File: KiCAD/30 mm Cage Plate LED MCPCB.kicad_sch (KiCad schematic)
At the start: 14 parts, among them IC1 AL8843QSP-13, J1 Conn_01x04

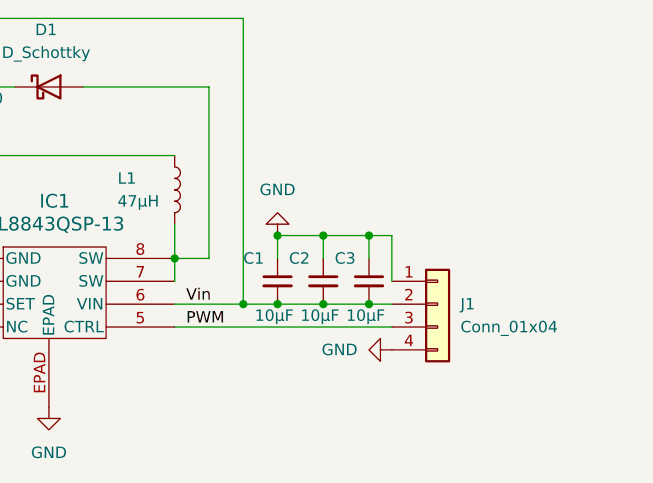
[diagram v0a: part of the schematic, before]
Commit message: Move PWM and Vin pins apart to prevent fatal shorts of Vin to Ctrl
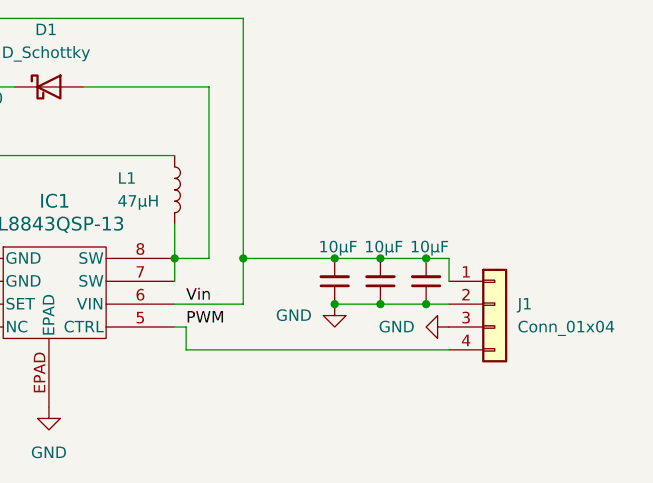
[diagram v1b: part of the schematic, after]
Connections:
- net GND: now also J1.2 (Pin_2), J1.3 (Pin_3); no longer J1.1 (Pin_1), J1.4 (Pin_4)
- net PWM: now also J1.4 (Pin_4); no longer J1.3 (Pin_3)
- net Vin: now also J1.1 (Pin_1); no longer J1.2 (Pin_2)
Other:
- moved on the sheet: J1

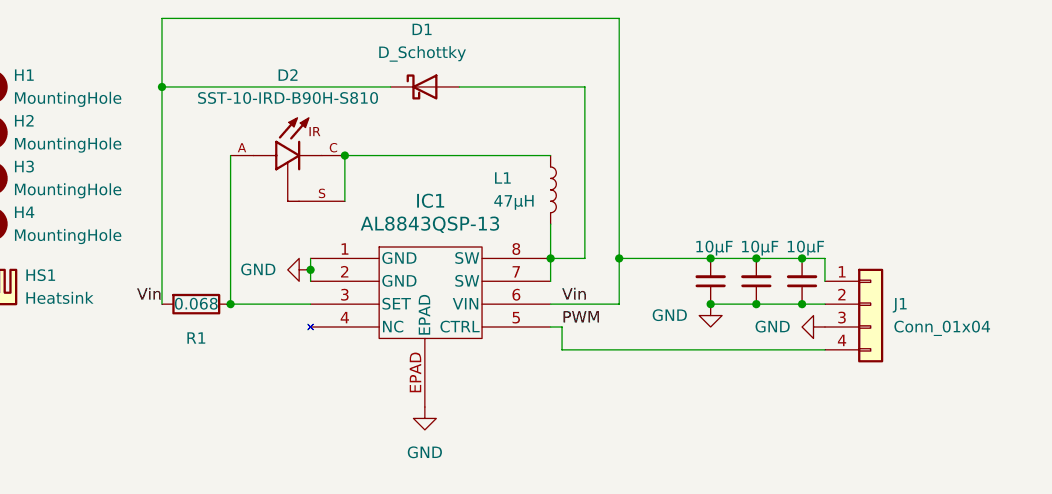
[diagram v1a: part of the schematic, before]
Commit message: Imrpoved design - more caps and therm
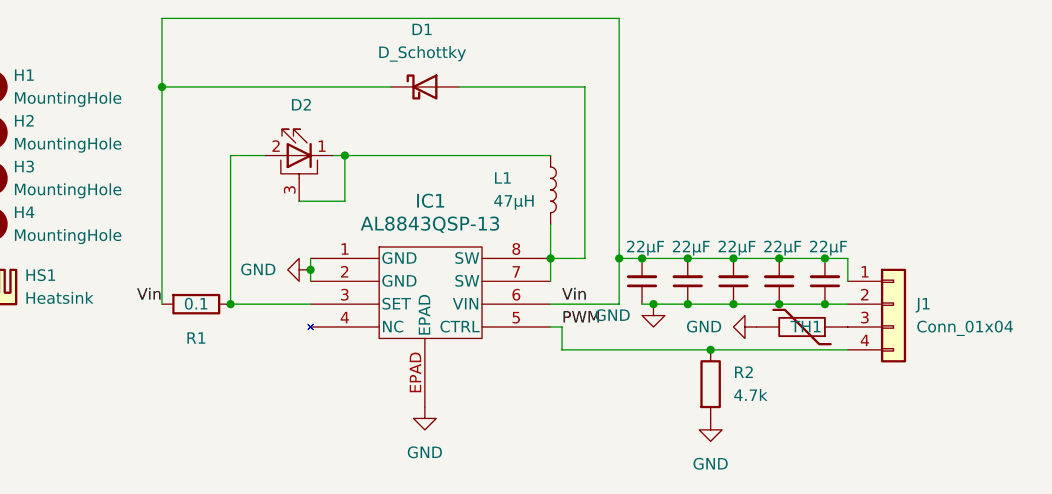
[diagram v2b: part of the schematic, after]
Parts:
- added C4, C5: 22µF, Capacitor_SMD:C_0805_2012Metric, symbol Device:C_Small
- added R2: 4.7k, Capacitor_SMD:C_0603_1608Metric, symbol Device:R
- added TH1: Thermistor, Resistor_SMD:R_0603_1608Metric, symbol Device:Thermistor
- C1, C2, C3: value 10μF -> 22µF; footprint Capacitor_SMD:C_0603_1608Metric -> Capacitor_SMD:C_0805_2012Metric; Manufacturer Murata Electronics -> Samsung Electro-Mechanics; Part GRM188R6YA106MA73D -> CL21A226MAYNNNE
- D2: footprint Custom:LED_SST-10-IRD-B90H-S810 -> Custom:CSSRML_C69062_AOS; symbol Custom:SST-10-IRD-B90H-S810 -> Device:LED_Pad; Manufacturer Luminus Devices Inc. -> ams-OSRAM USA INC.; Part SST-10-IRD-B90H-S810 -> GF CSSRML.24-TNUL-1-1-350-R33
- R1: value 0.068 -> 0.1; Manufacturer Ohmite -> Thin Film Technology Corp.; Part KDV12FR068ET -> D1WRL1206L4R100D-T5
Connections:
- net GND: now also C4.1, C5.1, R2.2, TH1.2; no longer J1.3 (Pin_3)
- net PWM: now also R2.1
- net Vin: now also C4.2, C5.2
- net at IC1.3 (SET), R1.1: now also D2.2 (A); no longer D2.A
- new net: J1.3 (Pin_3), TH1.1
- new net: D2.1 (K), D2.3 (PAD), L1.1
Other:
- moved on the sheet: J1

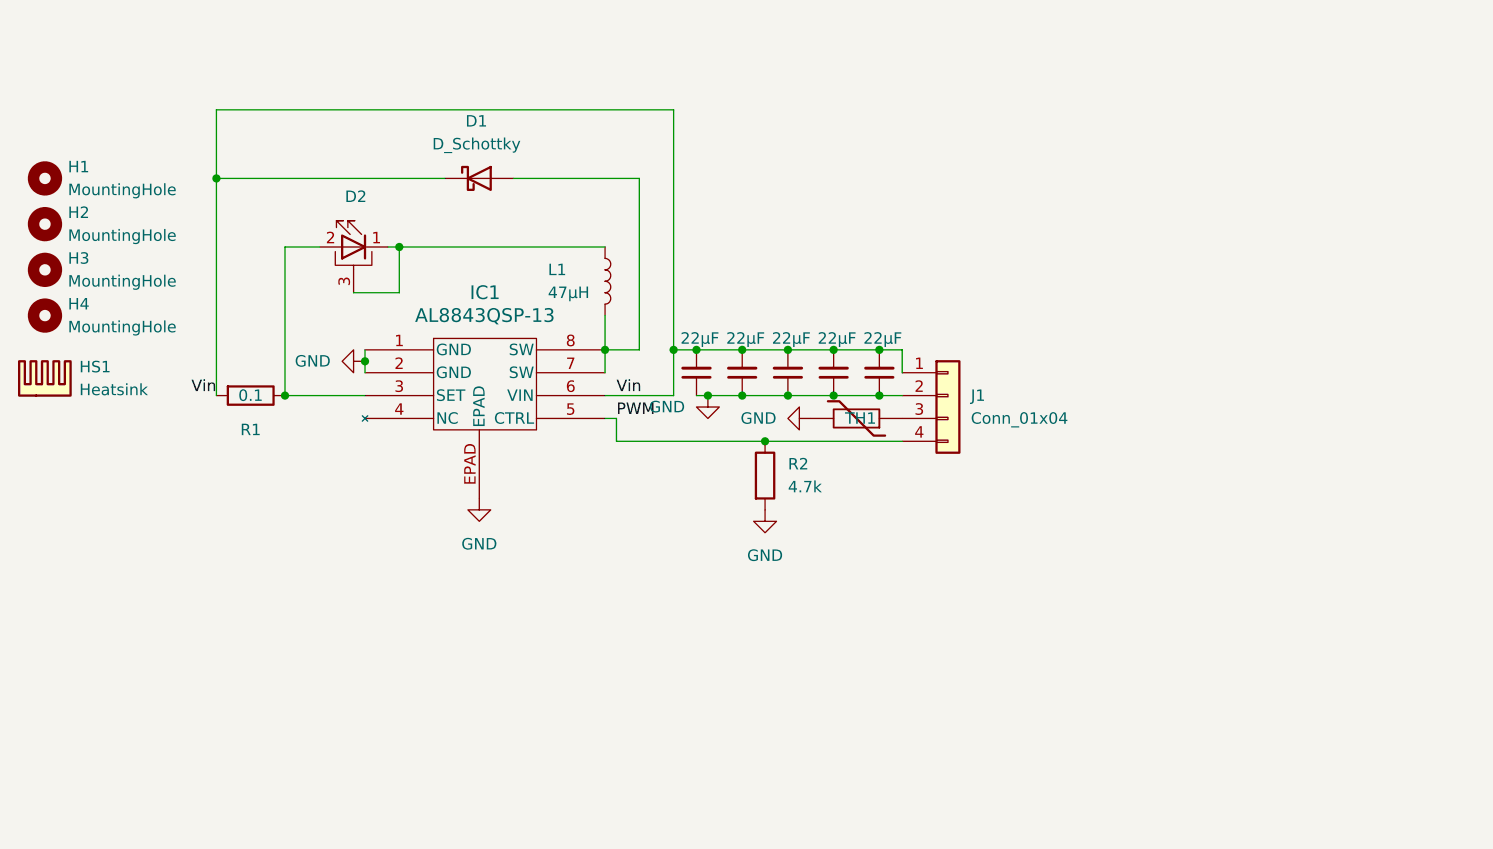
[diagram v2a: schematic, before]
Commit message: 60 mm plate with flat 8x connector
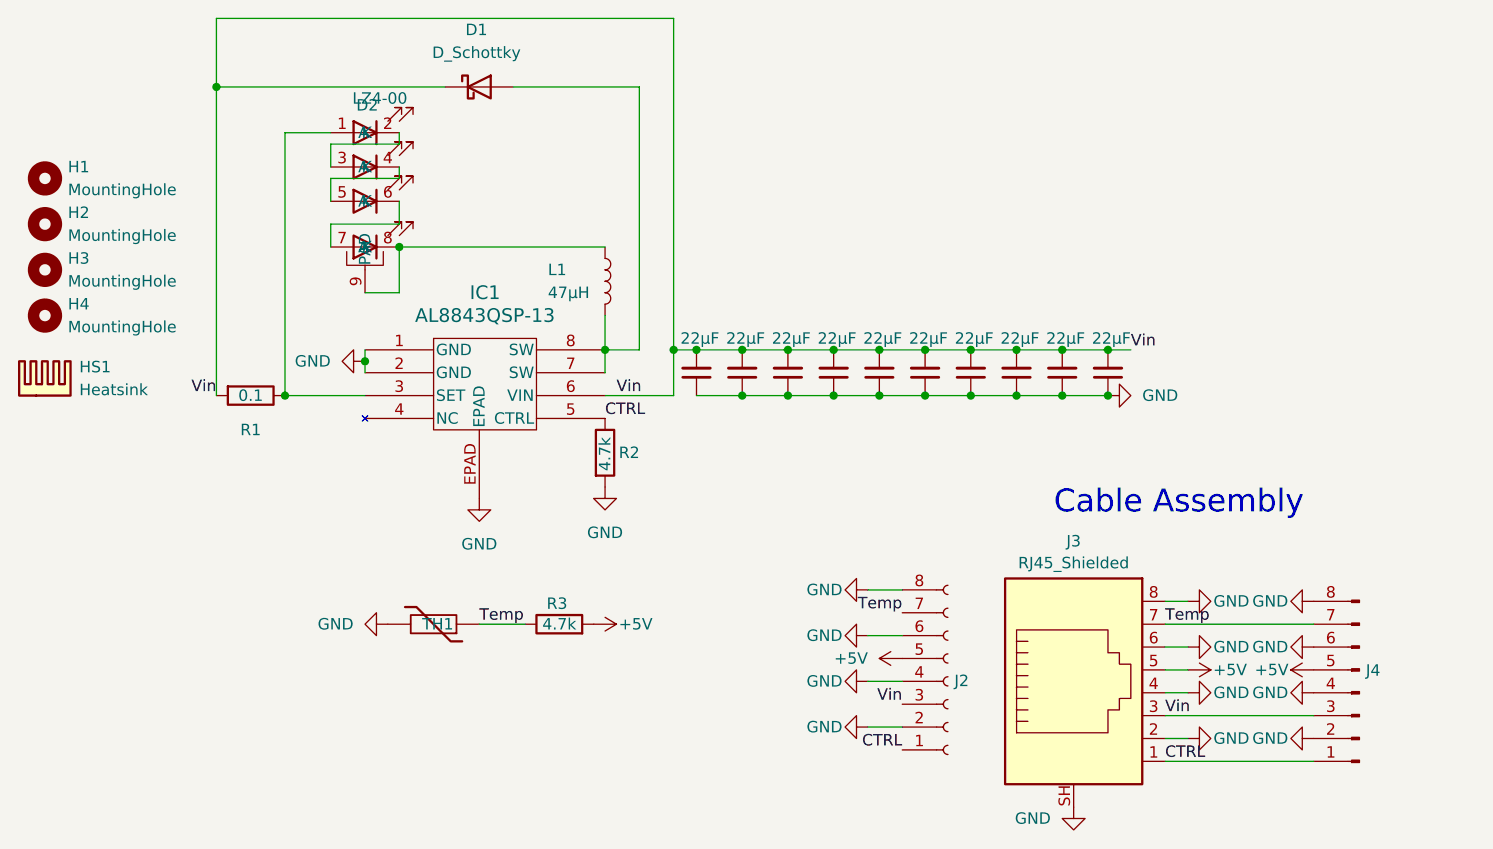
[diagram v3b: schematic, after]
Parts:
- removed D2: SST-10-IRD-B90H-S810, Custom:CSSRML_C69062_AOS, symbol Device:LED_Pad
- removed J1: Conn_01x04, Custom:SAMTEC_SSM-104-L-SH, symbol Connector_Generic:Conn_01x04
- added C10, C6, C7, C8, C9: 22µF, Capacitor_SMD:C_0805_2012Metric, symbol Device:C_Small
- added D2: LZ4-00, Custom:LZ4-00, symbol Custom:LZ4-00
- added J2: Conn_01x08_Socket, Custom:SAMTEC_SSM-108-F-SH-TR, symbol Connector:Conn_01x08_Socket
- added J3: RJ45_Shielded, symbol Connector:RJ45_Shielded
- added J4: Conn_01x08_Pin, symbol Connector:Conn_01x08_Pin
- added R3: 4.7k, Capacitor_SMD:C_0603_1608Metric, symbol Device:R
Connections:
- net GND: now also C10.1, C6.1, C7.1, C8.1, C9.1, J2.2 (Pin_2), J2.4 (Pin_4), J2.6 (Pin_6), J2.8 (Pin_8), J3.2, J3.4, J3.6, J3.8, J3.SH, J4.2 (Pin_2), J4.4 (Pin_4), J4.6 (Pin_6), J4.8 (Pin_8)
- net Vin: now also C10.2, C6.2, C7.2, C8.2, C9.2, J2.3 (Pin_3), J3.3, J4.3 (Pin_3)
- net Temp: now reaches TH1.1
- net Temp: now also J2.7 (Pin_7), J3.7, J4.7 (Pin_7), R3.1
- net at IC1.3 (SET), R1.1: now also D2.1 (A)
- net at L1.1: now also D2.8 (K), D2.9 (PAD)
- net PWM renamed CTRL
- net CTRL: now also J2.1 (Pin_1), J3.1, J4.1 (Pin_1)
- new net: D2.2 (K), D2.3 (A)
- new net: D2.4 (K), D2.5 (A)
- new net: D2.6 (K), D2.7 (A)
- new net +5V: J2.5 (Pin_5), J3.5, J4.5 (Pin_5), R3.2
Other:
- note added: "Cable Assembly"
- moved on the sheet: D1, R2, TH1

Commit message: CAD mockup
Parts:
- removed J2: Conn_01x08_Socket, Custom:SAMTEC_SSM-108-F-SH-TR, symbol Connector:Conn_01x08_Socket
- removed J4: Conn_01x08_Pin, symbol Connector:Conn_01x08_Pin
- removed R3: 4.7k, Capacitor_SMD:C_0603_1608Metric, symbol Device:R
- added J1: 8P8C_Shielded, Custom:1x RJ45, symbol Connector:8P8C_Shielded
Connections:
- net +5V is gone; now on net Vin: J3.5
- net CTRL: now also J3.7, J1.7; no longer J3.1
- net GND: now also J1.2, J1.4, J1.6, J1.8, J1.SH
- net Temp: now also J3.1, J1.1; no longer J3.7
- net Vin: now also J1.3, J1.5
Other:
- moved on the sheet: TH1

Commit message: Add T-cube connectivity
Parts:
- HS1: Manufacturer Wakefield-Vette -> Same Sky (Formerly CUI Devices); Part 906-31-1-23-2-B-0 -> HSB38-707025P
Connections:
- net GND: no longer J1.4, J3.4
- net Vin: no longer J1.3, J3.3
- net LED+: now reaches D2.1 (A), IC1.3 (SET), R1.1
- net LED+: now also J1.3, J3.3
- net LED-: now reaches D2.8 (K), D2.9 (PAD), L1.1
- net LED-: now also J1.4, J3.4
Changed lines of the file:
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@@
 	(wire
 		(pts
-			(xy 220.98 144.78) (xy 218.44 144.78)
+			(xy 218.44 144.78) (xy 234.95 144.78)
 		)
 		(stroke
@@
 		)
 	)
-	(label "Vin"
+	(label "LED+"
 		(at 218.44 147.32 0)
 		(fields_autoplaced yes)
@@
 		)
 	)
+	(label "LED+"
+		(at 125.73 82.55 180)
+		(fields_autoplaced yes)
+		(effects
+			(font
+				(size 1.27 1.27)
+			)
+			(justify right bottom)
+		)
+	)
 	(label "CTRL"
 		(at 156.21 114.3 0)
@@
 		)
 	)
+	(label "LED-"
+		(at 218.44 144.78 0)
+		(fields_autoplaced yes)
+		(effects
+			(font
+				(size 1.27 1.27)
+			)
+			(justify left bottom)
+		)
+	)
 	(label "Temp"
 		(at 218.44 152.4 0)
@@
 		)
 	)
+	(label "LED-"
+		(at 139.7 95.25 180)
+		(fields_autoplaced yes)
+		(effects
+			(font
+				(size 1.27 1.27)
+			)
+			(justify right bottom)
+		)
+	)
 	(label "Vin"
 		(at 218.44 142.24 0)
@@
 			)
 		)
-		(property "Datasheet" "LZ4-00"
+		(property "Datasheet" "https://look.ams-osram.com/m/60f2d29fa455f5ac/original/LZ4-00R308.pdf"
 			(at 129.54 80.01 0)
 			(effects
@@
 	(symbol
 		(lib_id "power:GND")
-		(at 234.95 144.78 270)
-		(mirror x)
-		(unit 1)
-		(exclude_from_sim no)
-		(in_bom yes)
-		(on_board yes)
-		(dnp no)
-		(property "Reference" "#PWR014"
-			(at 228.6 144.78 0)
-			(effects
-				(font
-					(size 1.27 1.27)
-				)
-				(hide yes)
-			)
-		)
-		(property "Value" "GND"
-			(at 230.124 144.78 90)
-			(effects
-				(font
-					(size 1.27 1.27)
-				)
-			)
-		)
-		(property "Footprint" ""
-			(at 234.95 144.78 0)
-			(effects
-				(font
-					(size 1.27 1.27)
-				)
-				(hide yes)
-			)
-		)
-		(property "Datasheet" ""
-			(at 234.95 144.78 0)
-			(effects
-				(font
-					(size 1.27 1.27)
-				)
-				(hide yes)
-			)
-		)
-		(property "Description" ""
-			(at 234.95 144.78 0)
-			(effects
-				(font
-					(size 1.27 1.27)
-				)
-				(hide yes)
-			)
-		)
-		(pin "1"
-		)
-		(instances
-			(project "30 mm Cage Plate LED MCPCB"
-				(path "/d4bfa918-6f2d-41e7-978b-b2160bded453"
-					(reference "#PWR014")
-					(unit 1)
-				)
-			)
-		)
-	)
-	(symbol
-		(lib_id "power:GND")
 		(at 129.54 107.95 270)
 		(unit 1)
@@
 			)
 		)
-		(property "Datasheet" "https://wakefieldthermal.com/content/data_sheets/ELLIPTICAL%20FIN%20HEAT%20SINK.pdf"
+		(property "Datasheet" "https://www.sameskydevices.com/product/resource/hsb38-707025p.pdf"
 			(at 94.2848 111.76 0)
 			(effects
@@
 			)
 		)
-		(property "Description" ""
+		(property "Description" "Heat Sink BGA Aluminum Alloy 21.7W @ 75°C Top Mount"
 			(at 93.98 111.76 0)
 			(effects
@@
 			)
 		)
-		(property "Manufacturer" "Wakefield-Vette"
+		(property "Manufacturer" "Same Sky (Formerly CUI Devices)"
 			(at 93.98 111.76 0)
 			(effects
@@
 			)
 		)
-		(property "Part" "906-31-1-23-2-B-0"
+		(property "Part" "HSB38-707025P"
 			(at 93.98 111.76 0)
 			(effects
@@
 					(unit 1)
 				)
-			)
-		)
-	)
-	(symbol
-		(lib_id "power:GND")
-		(at 220.98 144.78 90)
-		(mirror x)
-		(unit 1)
-		(exclude_from_sim no)
-		(in_bom yes)
-		(on_board yes)
-		(dnp no)
-		(property "Reference" "#PWR013"
-			(at 227.33 144.78 0)
-			(effects
-				(font
-					(size 1.27 1.27)
-				)
-				(hide yes)
-			)
-		)
-		(property "Value" "GND"
-			(at 225.806 144.78 90)
-			(effects
-				(font
-					(size 1.27 1.27)
-				)
-			)
-		)
-		(property "Footprint" ""
-			(at 220.98 144.78 0)
-			(effects
-				(font
-					(size 1.27 1.27)
-				)
-				(hide yes)
-			)
-		)
-		(property "Datasheet" ""
-			(at 220.98 144.78 0)
-			(effects
-				(font
-					(size 1.27 1.27)
-				)
-				(hide yes)
-			)
-		)
-		(property "Description" ""
-			(at 220.98 144.78 0)
-			(effects
-				(font
-					(size 1.27 1.27)
-				)
-				(hide yes)
-			)
-		)
-		(pin "1"
-		)
-		(instances
-			(project "30 mm Cage Plate LED MCPCB"
-				(path "/d4bfa918-6f2d-41e7-978b-b2160bded453"
-					(reference "#PWR013")
-					(unit 1)
-				)
